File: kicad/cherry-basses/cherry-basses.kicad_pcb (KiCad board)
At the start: 2 copper layers, 39 parts, among them SW1.1 SPST, SW1.2 SPST, SW1.3 SPST, SW1.4 SPST, SW1.5 SPST, SW1.6 SPST, SW1.7 SPST, SW1.8 SPST, SW2.0 SPST, SW2.1 SPST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

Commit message: Save cherry basses with kicad 6
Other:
- net class Default removed

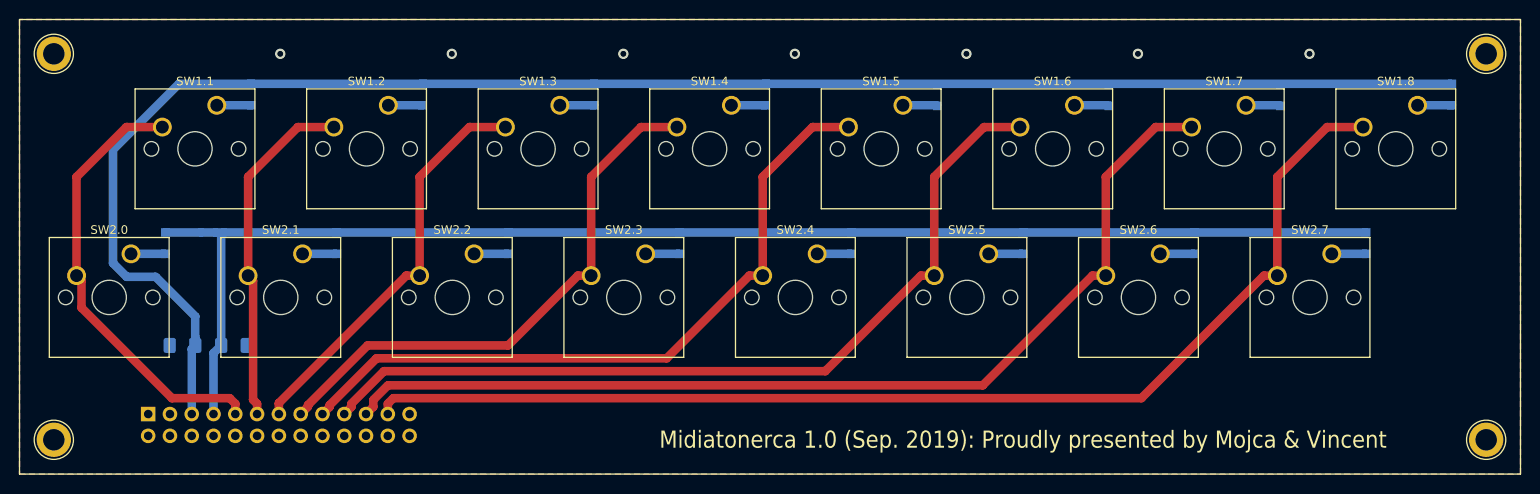
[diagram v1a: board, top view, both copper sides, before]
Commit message: Add edge cut to cherry basses
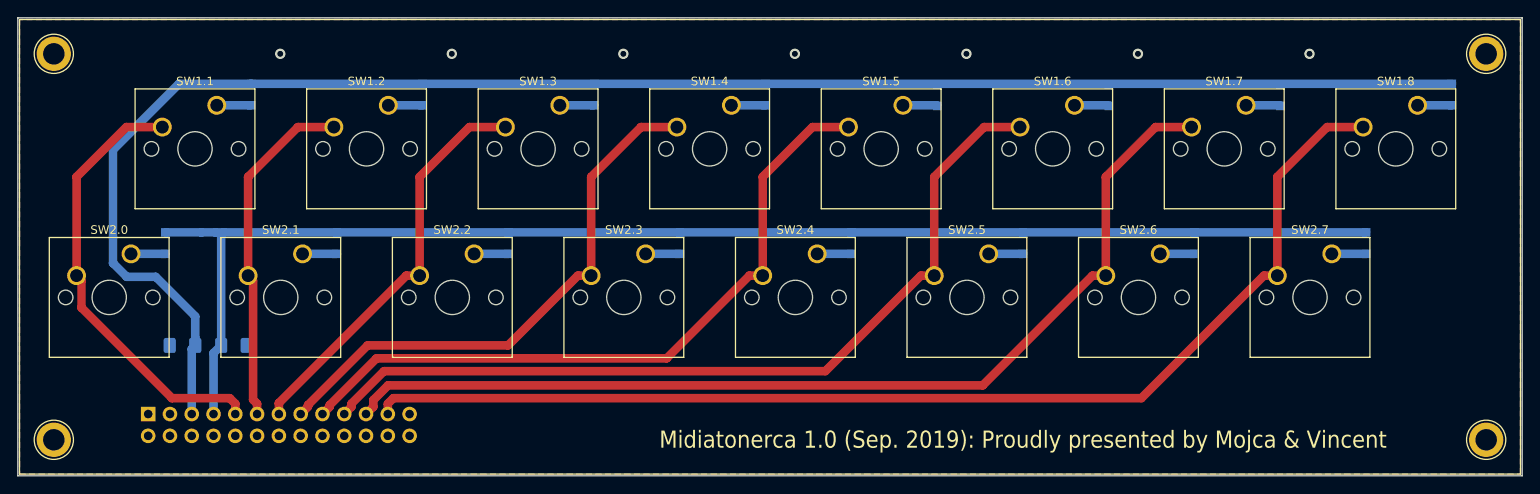
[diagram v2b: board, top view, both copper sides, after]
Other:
- board outline added: 175.4 x 53.4 mm
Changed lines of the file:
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@@
   (gr_line (start 222 40) (end 222 93) (layer "F.SilkS") (width 0.15))
   (gr_line (start 222 93) (end 47 93) (layer "F.SilkS") (width 0.15))
+  (gr_rect (start 46.8 39.8) (end 222.2 93.2) (layer "Edge.Cuts") (width 0.15) (fill none))
   (gr_text "Midiatonerca 1.0 (Sep. 2019): Proudly presented by Mojca & Vincent" (at 164 89) (layer "B.SilkS")
     (effects (font (size 2 1.8) (thickness 0.2)) (justify mirror))

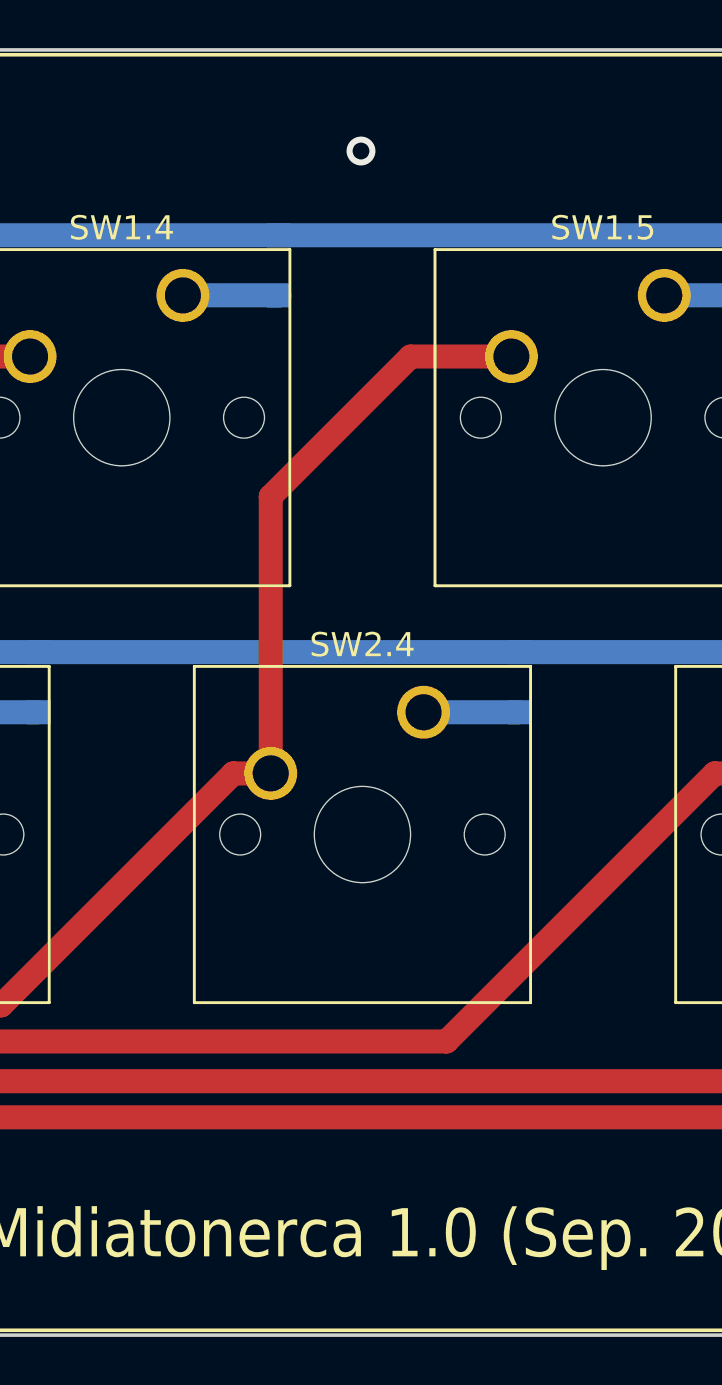
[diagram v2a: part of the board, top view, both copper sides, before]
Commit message: Add two mounting holes and refill background of cherry basses
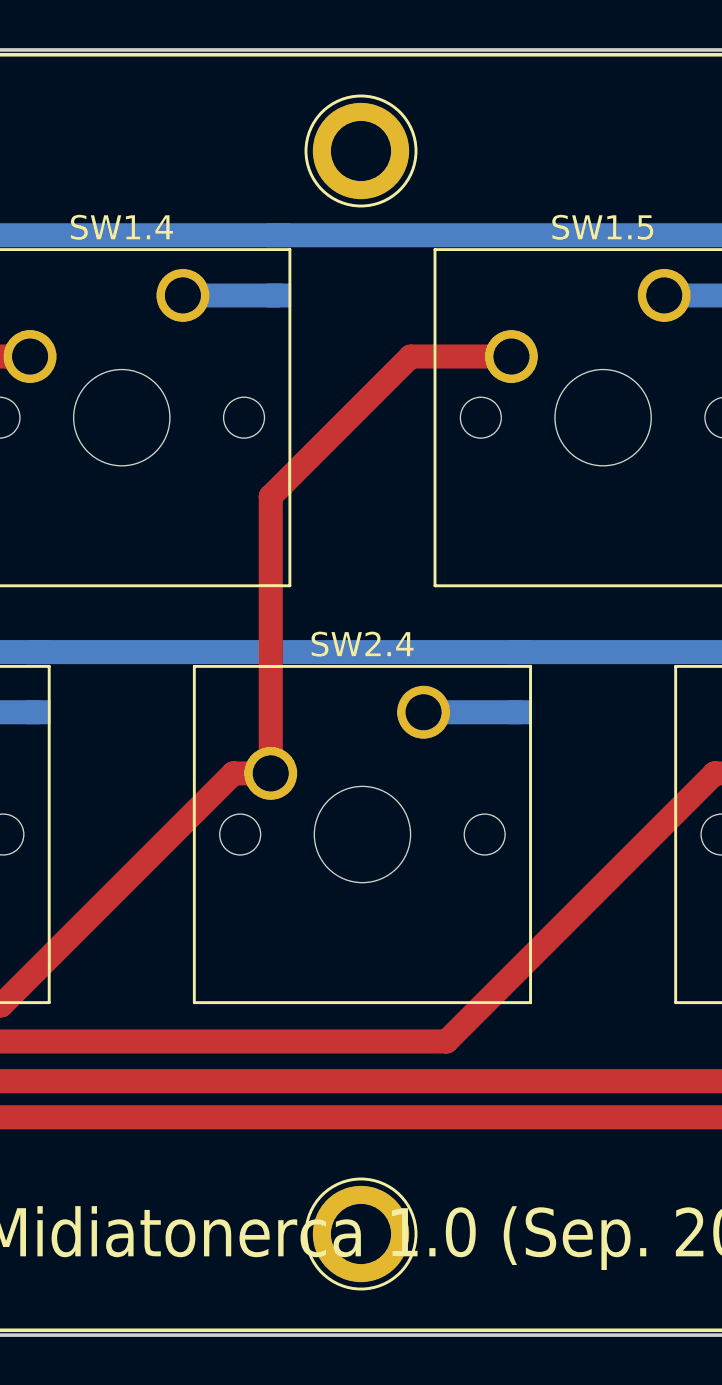
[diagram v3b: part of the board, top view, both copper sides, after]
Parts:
- added REF**: 1pin, Connectors:1pin, F.Cu at (137.4, 89.0)
- added REF**: 1pin, Connectors:1pin, F.Cu at (137.4, 44.0)
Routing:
- net (no net): vias 7 -> 6
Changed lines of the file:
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@@
+    (pad "1" thru_hole circle locked (at 0 0) (size 4 4) (drill 2.5) (layers *.Cu *.Mask))
+  )
+  (footprint "Connectors:1pin" (layer "F.Cu")
+    (at 137.4 89)
+    (descr "module 1 pin (ou trou mecanique de percage)")
+    (tags "DEV")
+    (attr through_hole)
+    (fp_text reference "REF**" (at 0 -3.048) (layer "F.SilkS") hide
+      (effects (font (size 1 1) (thickness 0.15)))
+    )
+    (fp_text value "1pin" (at 0 3) (layer "F.Fab") hide
+      (effects (font (size 1 1) (thickness 0.15)))
+    )
+    (fp_circle (center 0 0) (end 0 -2.286) (layer "F.SilkS") (width 0.12) (fill none))
+    (fp_circle (center 0 0) (end 2.6 0) (layer "F.CrtYd") (width 0.05) (fill none))
+    (fp_circle (center 0 0) (end 2 0.8) (layer "F.Fab") (width 0.1) (fill none))
+    (pad "1" thru_hole circle locked (at 0 0) (size 4 4) (drill 2.5) (layers *.Cu *.Mask))
+  )
+  (footprint "Connectors:1pin" (layer "F.Cu")
+    (at 137.4 44)
+    (descr "module 1 pin (ou trou mecanique de percage)")
+    (tags "DEV")
+    (attr through_hole)
+    (fp_text reference "REF**" (at 0 -3.048) (layer "F.SilkS") hide
+      (effects (font (size 1 1) (thickness 0.15)))
+    )
+    (fp_text value "1pin" (at 0 3) (layer "F.Fab") hide
+      (effects (font (size 1 1) (thickness 0.15)))
+    )
+    (fp_circle (center 0 0) (end 0 -2.286) (layer "F.SilkS") (width 0.12) (fill none))
+    (fp_circle (center 0 0) (end 2.6 0) (layer "F.CrtYd") (width 0.05) (fill none))
+    (fp_circle (center 0 0) (end 2 0.8) (layer "F.Fab") (width 0.1) (fill none))
     (pad "1" thru_hole circle locked (at 0 0) (size 4 4) (drill 2.5) (layers *.Cu *.Mask))
   )
@@
   (via (at 97.4 44) (size 1.2) (drill 0.7) (layers "F.Cu" "B.Cu") (net 0))
   (via (at 117.4 44) (size 1.2) (drill 0.7) (layers "F.Cu" "B.Cu") (net 0))
-  (via (at 137.4 44) (size 1.2) (drill 0.7) (layers "F.Cu" "B.Cu") (net 0))
   (via (at 157.4 44) (size 1.2) (drill 0.7) (layers "F.Cu" "B.Cu") (net 0))
   (via (at 177.4 44) (size 1.2) (drill 0.7) (layers "F.Cu" "B.Cu") (net 0))
@@
   (zone (net 27) (net_name "GND") (layer "F.Cu") (hatch edge 0.508)
     (connect_pads (clearance 0.508))
-    (min_thickness 0.254)
+    (min_thickness 0.254) (filled_areas_thickness no)
     (fill yes (thermal_gap 0.508) (thermal_bridge_width 0.508))
     (polygon
@@
   (zone (net 27) (net_name "GND") (layer "B.Cu") (hatch edge 0.508)
     (connect_pads (clearance 0.508))
-    (min_thickness 0.254)
+    (min_thickness 0.254) (filled_areas_thickness no)
     (fill yes (thermal_gap 0.508) (thermal_bridge_width 0.508))
     (polygon

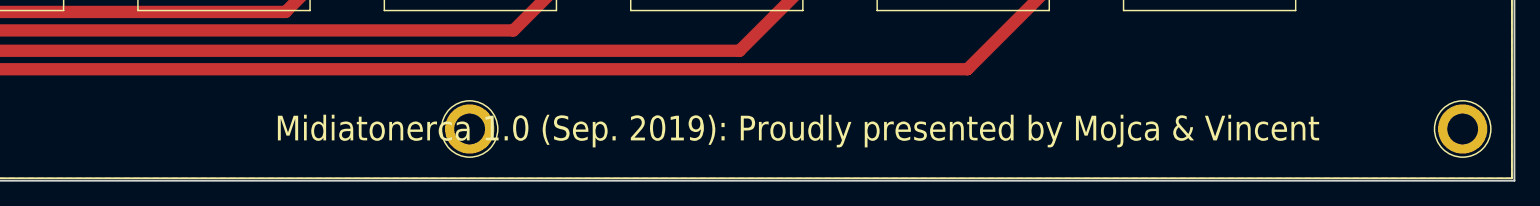
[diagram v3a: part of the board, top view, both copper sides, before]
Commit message: Fix silkscreen text on cherry basses
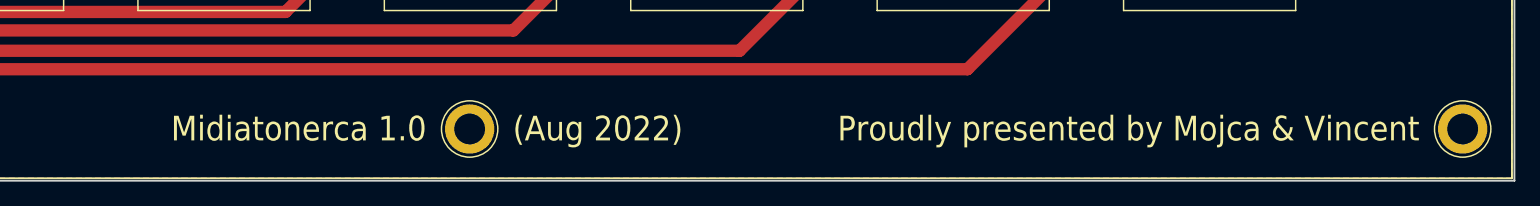
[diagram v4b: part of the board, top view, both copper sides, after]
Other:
- board text added: "(Aug 2022)"
- board text added: "Midiatonerca 1.0"
- board text added: "Proudly presented by Mojca & Vincent"
- board text removed: "Midiatonerca 1.0 (Sep. 2019): Proudly presented by Mojca & Vincent"
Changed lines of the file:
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@@
   (gr_line (start 222 93) (end 47 93) (layer "F.SilkS") (width 0.15))
   (gr_rect (start 46.8 39.8) (end 222.2 93.2) (layer "Edge.Cuts") (width 0.15) (fill none))
-  (gr_text "Midiatonerca 1.0 (Sep. 2019): Proudly presented by Mojca & Vincent" (at 164 89) (layer "B.SilkS")
-    (effects (font (size 2 1.8) (thickness 0.2)) (justify mirror))
+  (gr_text "Midiatonerca 1.0" (at 133.9 89) (layer "B.SilkS")
+    (effects (font (size 2 1.8) (thickness 0.2)) (justify left mirror))
   )
-  (gr_text "Midiatonerca 1.0 (Sep. 2019): Proudly presented by Mojca & Vincent" (at 164 89) (layer "F.SilkS")
-    (effects (font (size 2 1.8) (thickness 0.2)))
+  (gr_text "(Aug 2022)" (at 140.9 89) (layer "B.SilkS")
+    (effects (font (size 2 1.8) (thickness 0.2)) (justify right mirror))
+  )
+  (gr_text "Proudly presented by Mojca & Vincent" (at 214.5 89) (layer "B.SilkS")
+    (effects (font (size 2 1.8) (thickness 0.2)) (justify left mirror))
+  )
+  (gr_text "Proudly presented by Mojca & Vincent" (at 214.5 89) (layer "F.SilkS")
+    (effects (font (size 2 1.8) (thickness 0.2)) (justify right))
+  )
+  (gr_text "(Aug 2022)" (at 140.9 89) (layer "F.SilkS")
+    (effects (font (size 2 1.8) (thickness 0.2)) (justify left))
+  )
+  (gr_text "Midiatonerca 1.0" (at 133.9 89) (layer "F.SilkS")
+    (effects (font (size 2 1.8) (thickness 0.2)) (justify right))
   )
   (via (at 97.4 44) (size 1.2) (drill 0.7) (layers "F.Cu" "B.Cu") (net 0))

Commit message: cherry basses pcb: no clue what changed
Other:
- rule pad_to_mask_clearance: 0.051 -> 0
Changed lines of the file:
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@@
   )
   (setup
-    (pad_to_mask_clearance 0.051)
-    (solder_mask_min_width 0.25)
+    (pad_to_mask_clearance 0)
     (pcbplotparams
       (layerselection 0x00010fc_ffffffff)
@@
     (fp_line (start -1.6 0.8) (end 1.6 0.8) (layer "B.Fab") (width 0.1))
     (fp_line (start -1.6 -0.8) (end -1.6 0.8) (layer "B.Fab") (width 0.1))
-    (pad "1" smd roundrect locked (at -1.4875 0 180) (size 1.425 1.75) (layers "B.Cu" "B.Paste" "B.Mask") (roundrect_rratio 0.175439)
+    (pad "1" smd roundrect locked (at -1.4875 0 180) (size 1.425 1.75) (layers "B.Cu" "B.Paste" "B.Mask") (roundrect_rratio 0.1754392982)
       (net 13 "arduino_D3"))
-    (pad "2" smd roundrect locked (at 1.4875 0 180) (size 1.425 1.75) (layers "B.Cu" "B.Paste" "B.Mask") (roundrect_rratio 0.175439)
+    (pad "2" smd roundrect locked (at 1.4875 0 180) (size 1.425 1.75) (layers "B.Cu" "B.Paste" "B.Mask") (roundrect_rratio 0.1754392982)
       (net 27 "GND"))
     (model "${KISYS3DMOD}/Resistor_SMD.3dshapes/R_1206_3216Metric.wrl"
@@
     (fp_line (start -1.6 0.8) (end 1.6 0.8) (layer "B.Fab") (width 0.1))
     (fp_line (start 1.6 0.8) (end 1.6 -0.8) (layer "B.Fab") (width 0.1))
-    (pad "1" smd roundrect locked (at -1.4875 0) (size 1.425 1.75) (layers "B.Cu" "B.Paste" "B.Mask") (roundrect_rratio 0.175439)
+    (pad "1" smd roundrect locked (at -1.4875 0) (size 1.425 1.75) (layers "B.Cu" "B.Paste" "B.Mask") (roundrect_rratio 0.1754392982)
       (net 15 "arduino_D4"))
-    (pad "2" smd roundrect locked (at 1.4875 0) (size 1.425 1.75) (layers "B.Cu" "B.Paste" "B.Mask") (roundrect_rratio 0.175439)
+    (pad "2" smd roundrect locked (at 1.4875 0) (size 1.425 1.75) (layers "B.Cu" "B.Paste" "B.Mask") (roundrect_rratio 0.1754392982)
       (net 27 "GND"))
     (model "${KISYS3DMOD}/Resistor_SMD.3dshapes/R_1206_3216Metric.wrl"

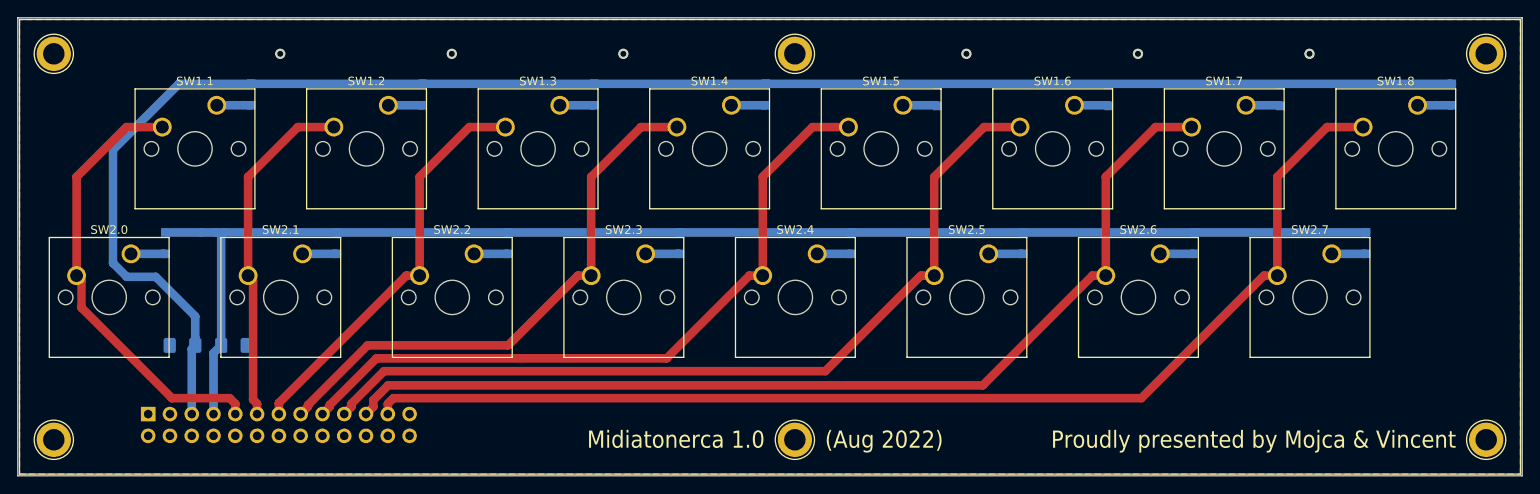
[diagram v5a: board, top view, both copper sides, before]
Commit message: Update pcb for cherry basses
- add connector for the side button
- fix vias
- fix positions of some diodes
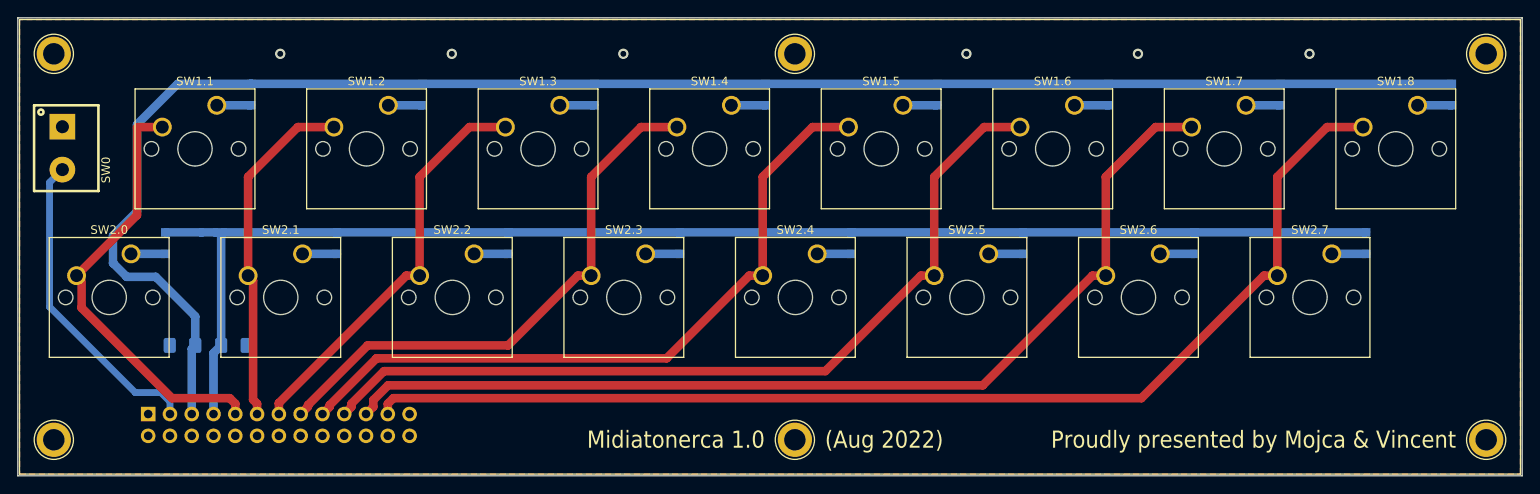
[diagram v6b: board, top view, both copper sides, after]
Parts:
- added SW0: SPST, Library:Neltron-5523S-XX-10-X-Terminal-P5.0mm-7.5x10, F.Cu at (52.0, 55.0)
- moved D1.5 0.08 mm to (154.0, 48.8)
- moved D1.6 0.08 mm to (174.0, 48.8)
- moved D1.7 0.08 mm to (194.0, 48.8)
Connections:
- Conn1 pad 1: (no net) -> unconnected-(Conn1-Pad1)
- Conn1 pad 10: (no net) -> unconnected-(Conn1-Pad10)
- Conn1 pad 12: (no net) -> unconnected-(Conn1-Pad12)
- Conn1 pad 14: (no net) -> unconnected-(Conn1-Pad14)
- Conn1 pad 16: (no net) -> unconnected-(Conn1-Pad16)
- Conn1 pad 18: (no net) -> unconnected-(Conn1-Pad18)
- Conn1 pad 2: (no net) -> unconnected-(Conn1-Pad2)
- Conn1 pad 20: (no net) -> unconnected-(Conn1-Pad20)
- Conn1 pad 22: (no net) -> unconnected-(Conn1-Pad22)
- Conn1 pad 24: (no net) -> unconnected-(Conn1-Pad24)
- Conn1 pad 3: (no net) -> arduino_D2
- Conn1 pad 4: (no net) -> unconnected-(Conn1-Pad4)
- Conn1 pad 6: (no net) -> unconnected-(Conn1-Pad6)
- Conn1 pad 8: (no net) -> unconnected-(Conn1-Pad8)
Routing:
- net arduino_D2: track 0.00 -> 36.7 mm
- net arduino_D5: track 51.7 -> 50.1 mm
- net GND: vias 0 -> 6
- net (no net): vias 6 -> 0
